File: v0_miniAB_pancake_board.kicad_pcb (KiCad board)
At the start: 2 copper layers, 51 x 37.4 mm, 13 parts, among them J1 Conn_01x04_Female, J10 Conn_01x03_Female, J11 Conn_01x03_Female, J2 Conn_01x02_Female, J3 Conn_01x02_Female, J4 Conn_01x02_Female, J5 Conn_01x02_Female, J6 Conn_01x02_Female, J7 Conn_01x03_Female, J8 Conn_01x03_Female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

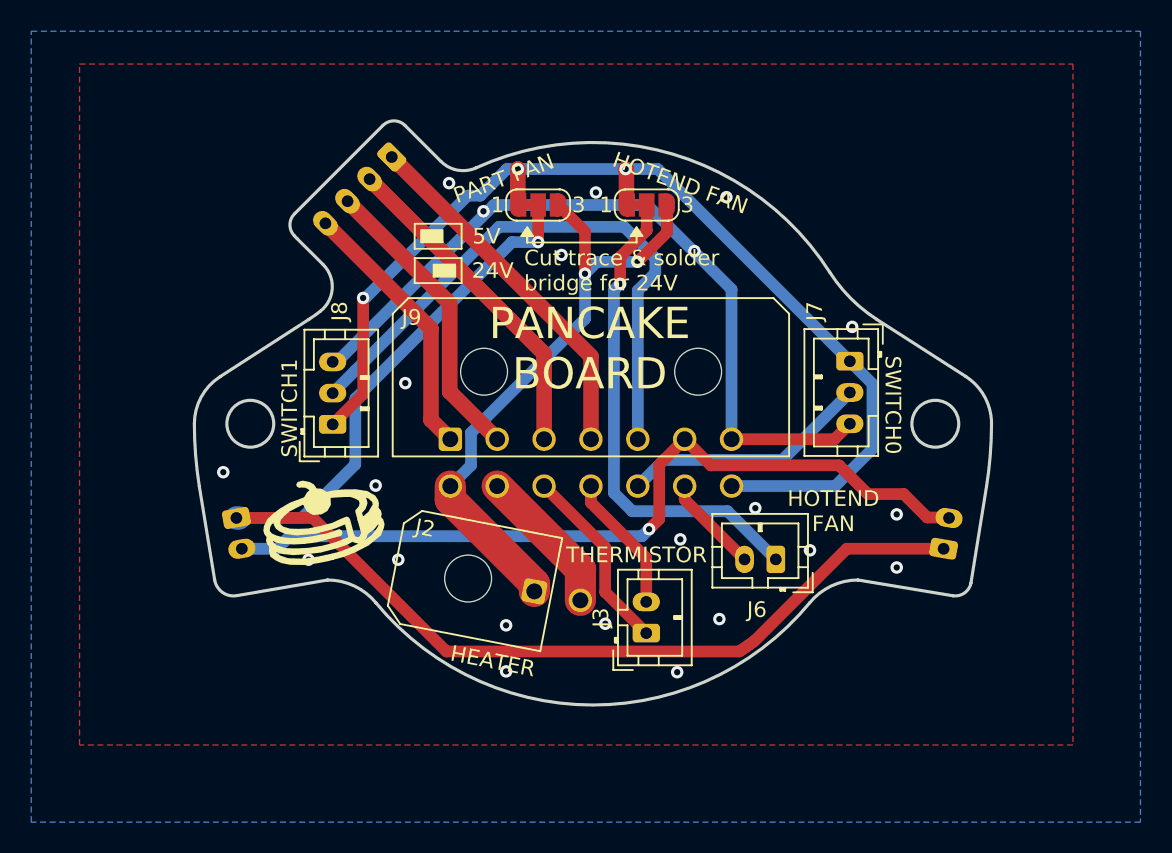
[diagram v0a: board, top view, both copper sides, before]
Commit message: Converted to KiCAD 6.0.0
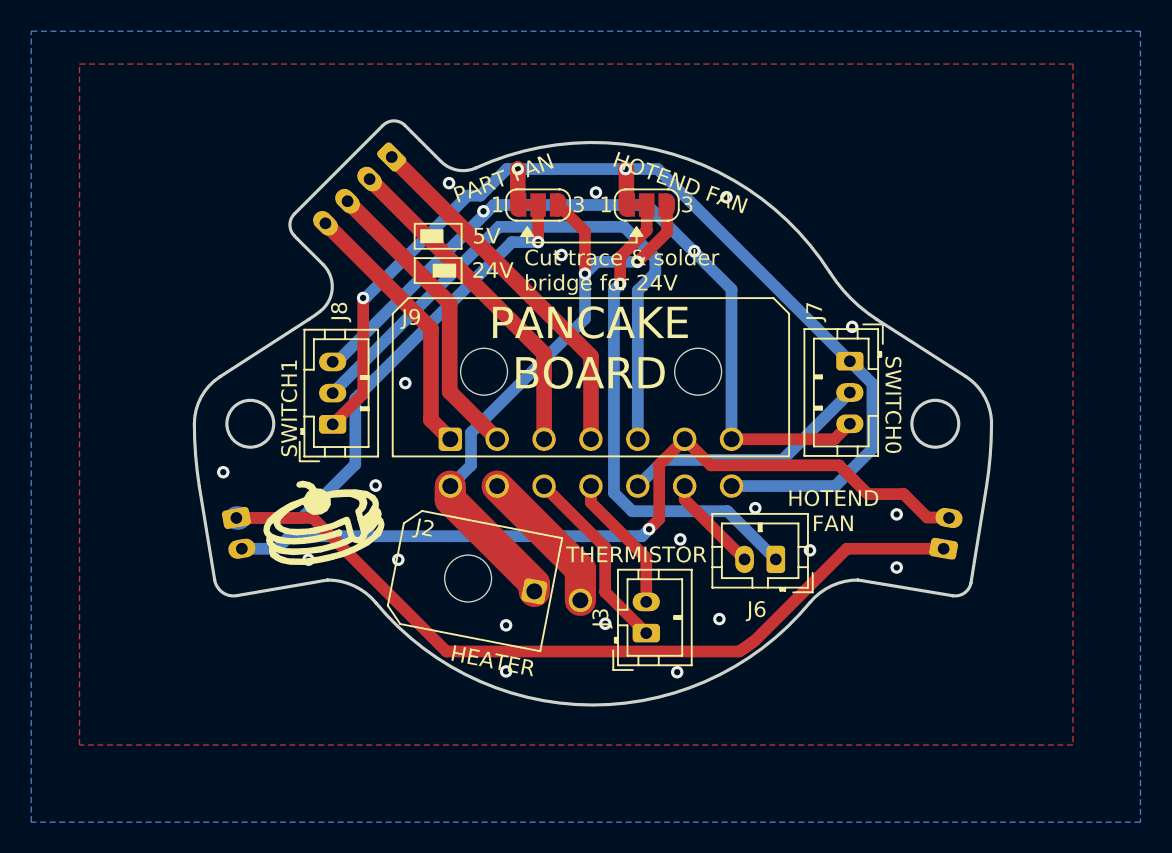
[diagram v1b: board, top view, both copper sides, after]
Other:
- net class Default removed

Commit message: First steps of the batboard conversion
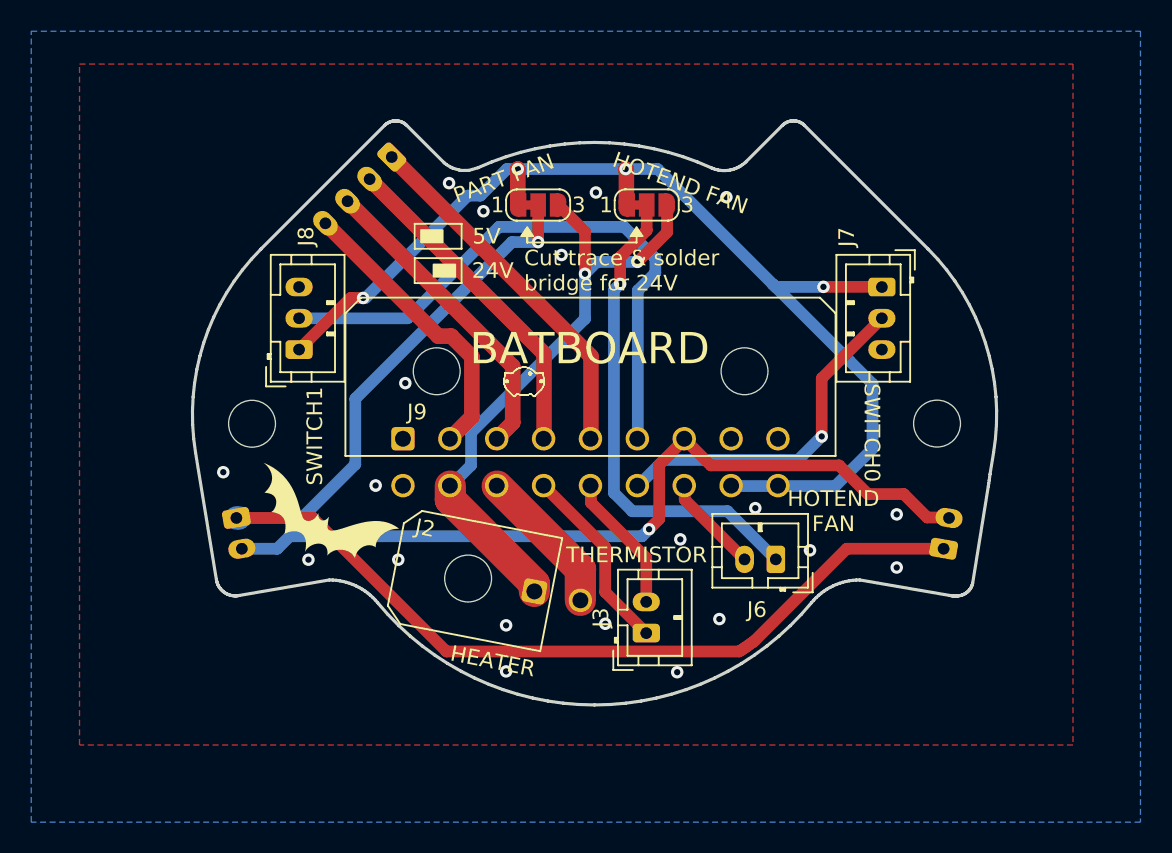
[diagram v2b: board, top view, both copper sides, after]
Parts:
- removed the REF** at (80.0, 110.7)
- removed the REF** at (89.4, 108.5)
- added REF**: MountingHole_3mm, MountingHole:MountingHole_3mm, F.Cu at (122.0, 100.0)
- added REF**: MountingHole_3mm, MountingHole:MountingHole_3mm, F.Cu at (78.2, 100.0)
- added svg2mod: G***, logos:Bat_Logo, F.Cu at (78.9, 101.2)
- added svg2mod: G***, logos:Bat_Logo, B.Cu at (90.5, 110.2)
- J9: footprint Connector_Molex:Molex_Micro-Fit_3.0_43045-1400_2x07_P3.00mm_Horizontal -> Connector_Molex:Molex_Micro-Fit_3.0_43045-1800_2x09_P3.00mm_Horizontal
- moved J8 5.25 mm to (81.2, 95.2)
- moved J7 5.17 mm to (118.5, 91.2)
- moved J9 3.03 mm to (87.8, 101.0)
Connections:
- J9 pad 1: /A+ -> unconnected-(J9-Pad1)
- J9 pad 10: /therm0 -> unconnected-(J9-Pad10)
- J9 pad 11: /therm1 -> +24V
- J9 pad 12: /sw0 -> /heat_gnd
- J9 pad 13: /fan1 -> /therm0
- J9 pad 14: +5V -> /therm1
- J9 pad 2: /A- -> /A+
- J9 pad 3: /B+ -> /A-
- J9 pad 4: /B- -> /B+
- J9 pad 5: /sw1 -> /B-
- J9 pad 6: /fan0 -> /sw1
- J9 pad 7: GND -> /fan0
- J9 pad 8: +24V -> GND
- J9 pad 9: /heat_gnd -> unconnected-(J9-Pad9)
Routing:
- net GND: track 49.6 -> 0.05 mm, vias 22 -> 20
- net /sw0: track 16.1 -> 22.2 mm, vias 0 -> 1
- net +5V: track 69.4 -> 73.0 mm, vias 3 -> 4
- net /A+: track 17.1 -> 18.7 mm
- net /A-: track 19.2 -> 20.0 mm
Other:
- board size 51 x 37.4 mm -> 51.5 x 37.4 mm
- board text added: "(based on Pancake by Christoph Mueller)"
- board text added: "BATBOARD"
- board text removed: "PANCAKE BOARD"
- board text removed: "christophmueller.org 2021"

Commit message: Further connections made
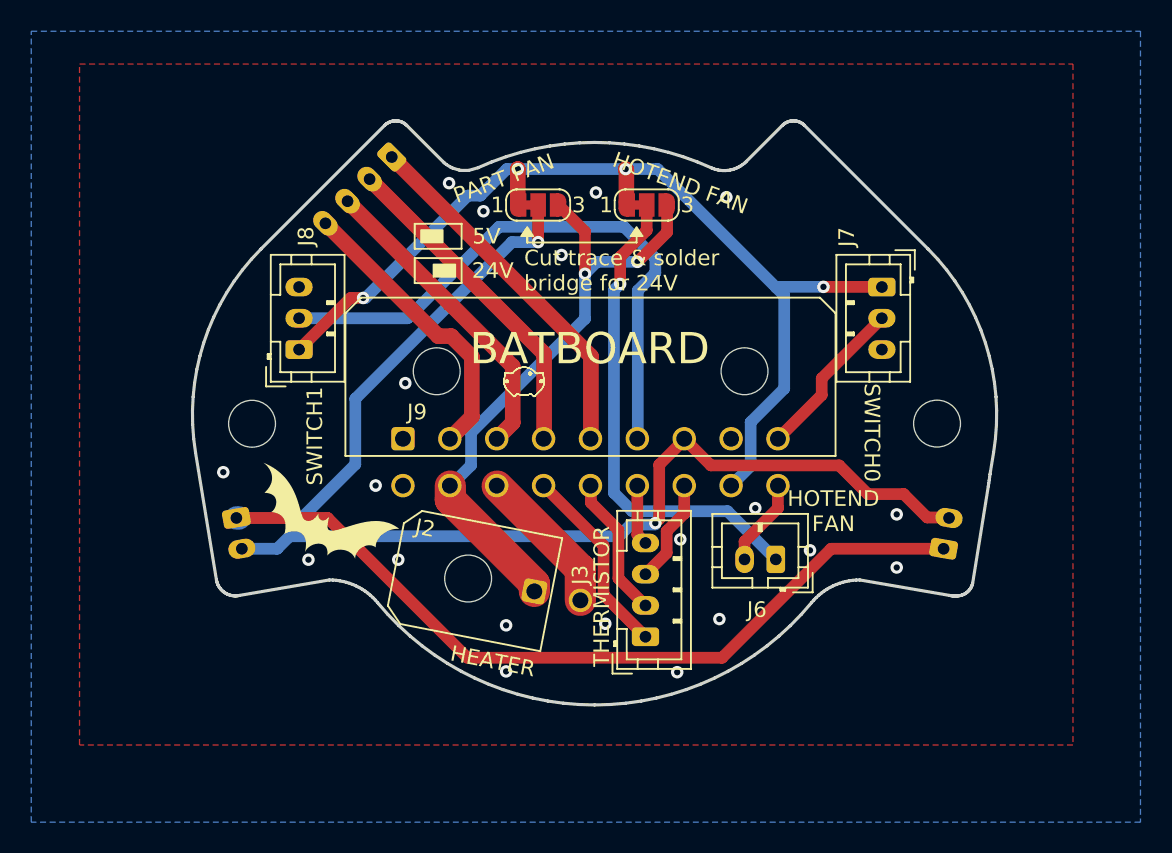
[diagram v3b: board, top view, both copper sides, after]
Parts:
- J3: value Conn_01x02_Female -> Conn_01x04_Female; footprint Connector_JST:JST_PH_B2B-PH-K_1x02_P2.00mm_Vertical -> Connector_JST:JST_PH_B4B-PH-K_1x04_P2.00mm_Vertical
- moved J3 0.24 mm to (103.4, 113.6)
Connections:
- J9 pad 15: /sw0 -> /therm3
- J9 pad 16: /fan1 -> /therm2
- J9 pad 18: unconnected-(J9-Pad18) -> /fan1
- J9 pad 9: unconnected-(J9-Pad9) -> /sw0
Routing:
- net /VFAN1: track 31.4 -> 0.00 mm, vias 1 -> 0
- net /fan0: track 52.3 -> 83.7 mm, vias 1 -> 2
- net /sw0: track 22.2 -> 10.5 mm, vias 1 -> 0
- net +5V: track 73.0 -> 64.0 mm
- net /therm2: track 0.00 -> 6.70 mm
- net /therm3: track 0.00 -> 3.89 mm
- net /fan1: track 6.28 -> 5.61 mm

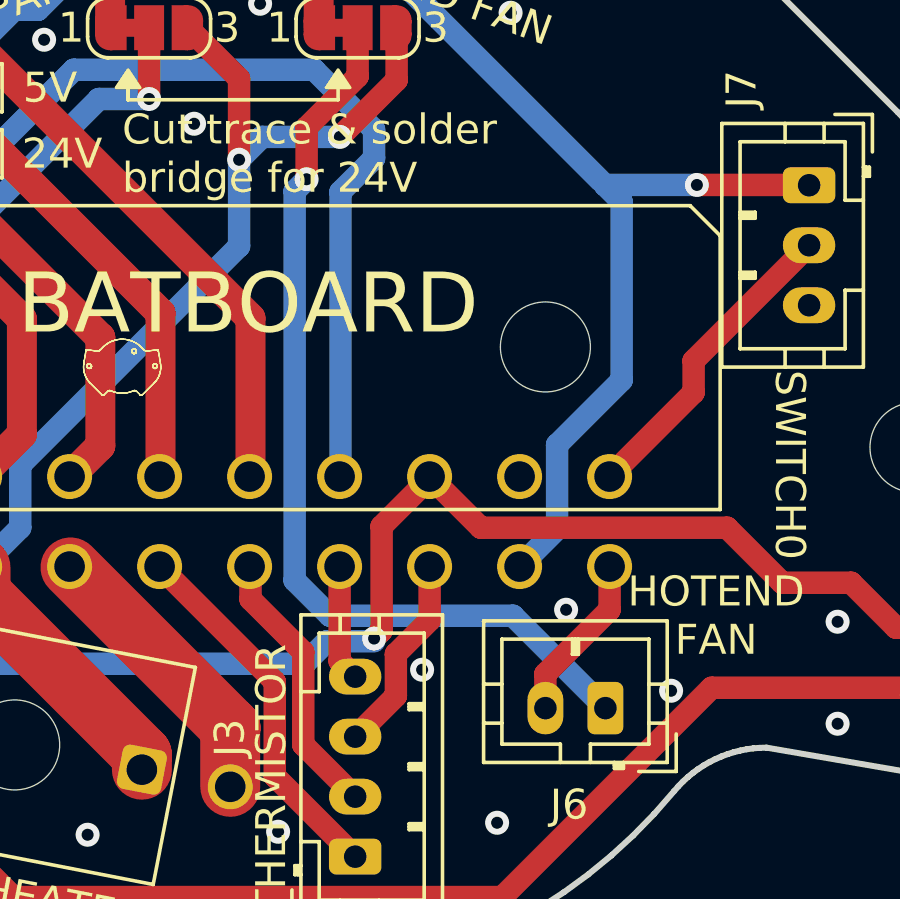
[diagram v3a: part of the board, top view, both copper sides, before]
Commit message: Fixed track to VFAN1
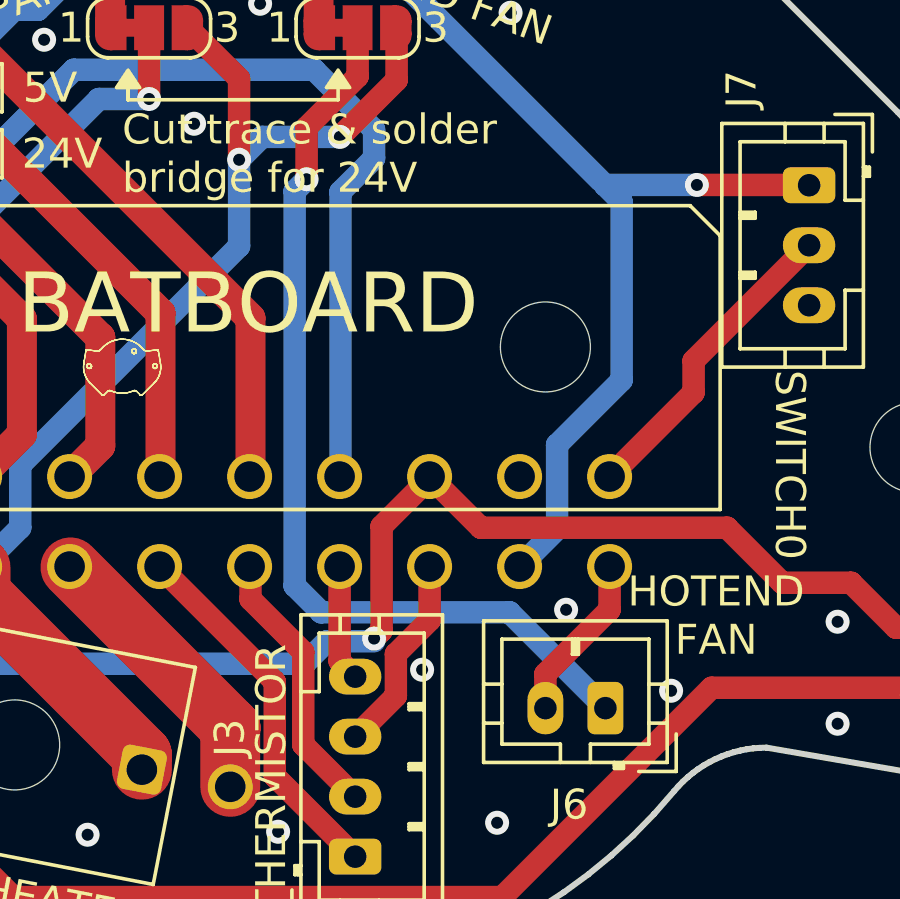
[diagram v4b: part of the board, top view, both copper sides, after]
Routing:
- net /VFAN1: track 0.00 -> 31.5 mm, vias 0 -> 1
- net /fan0: track 83.7 -> 52.3 mm, vias 2 -> 1
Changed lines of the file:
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@@
   (segment (start 117.6 104.5) (end 115.764999 102.664999) (width 0.75) (layer "F.Cu") (net 7))
   (segment (start 105.88 100.99) (end 104.249999 102.620001) (width 0.75) (layer "F.Cu") (net 7))
-  (segment (start 103.45 87.623401) (end 101.75 89.323401) (width 0.75) (layer "F.Cu") (net 7))
-  (segment (start 103.45 86) (end 103.45 87.623401) (width 0.75) (layer "F.Cu") (net 7))
   (segment (start 122.766912 106) (end 121.4 106) (width 0.75) (layer "F.Cu") (net 7))
   (segment (start 115.764999 102.664999) (end 107.554999 102.664999) (width 0.75) (layer "F.Cu") (net 7))
@@
   (segment (start 119.9 104.5) (end 117.6 104.5) (width 0.75) (layer "F.Cu") (net 7))
   (segment (start 122.797296 106.030384) (end 122.766912 106) (width 0.75) (layer "F.Cu") (net 7))
-  (segment (start 101.75 89.323401) (end 101.75 91.05) (width 0.75) (layer "F.Cu") (net 7))
   (segment (start 121.4 106) (end 119.9 104.5) (width 0.75) (layer "F.Cu") (net 7))
   (via (at 104 106.36) (size 0.8) (drill 0.4) (layers "F.Cu" "B.Cu") (net 7))
-  (via (at 101.75 91.05) (size 0.8) (drill 0.4) (layers "F.Cu" "B.Cu") (net 7))
   (segment (start 102.43048 106.44952) (end 104 106.44952) (width 0.75) (layer "B.Cu") (net 7))
-  (segment (start 101.350001 91.449999) (end 101.350001 104.421003) (width 0.75) (layer "B.Cu") (net 7))
-  (segment (start 101.350001 104.421003) (end 102.528998 105.6) (width 0.75) (layer "B.Cu") (net 7))
-  (segment (start 108.63 105.6) (end 111.71 108.68) (width 0.75) (layer "B.Cu") (net 7))
   (segment (start 80.6 107.2) (end 101.68 107.2) (width 0.75) (layer "B.Cu") (net 7))
-  (segment (start 102.528998 105.6) (end 108.63 105.6) (width 0.75) (layer "B.Cu") (net 7))
   (segment (start 101.68 107.2) (end 102.43048 106.44952) (width 0.75) (layer "B.Cu") (net 7))
   (segment (start 77.537296 107.999616) (end 79.800384 107.999616) (width 0.75) (layer "B.Cu") (net 7))
   (segment (start 79.800384 107.999616) (end 80.6 107.2) (width 0.75) (layer "B.Cu") (net 7))
-  (segment (start 101.75 91.05) (end 101.350001 91.449999) (width 0.75) (layer "B.Cu") (net 7))
   (segment (start 95.2 83.700006) (end 95.199994 83.7) (width 1) (layer "F.Cu") (net 8))
   (segment (start 118.49 91.24) (end 118.5 91.25) (width 0.75) (layer "F.Cu") (net 8))
@@
   (segment (start 84.80001 102.59999) (end 84.80001 98.39999) (width 0.75) (layer "B.Cu") (net 15))
   (segment (start 77.19 106.03) (end 77.36 106.03) (width 1.5) (layer "B.Cu") (net 15))
+  (segment (start 103.45 87.623401) (end 101.75 89.323401) (width 0.75) (layer "F.Cu") (net 16))
+  (segment (start 103.45 86) (end 103.45 87.623401) (width 0.75) (layer "F.Cu") (net 16))
+  (segment (start 101.75 89.323401) (end 101.75 91.05) (width 0.75) (layer "F.Cu") (net 16))
+  (via (at 101.75 91.05) (size 0.8) (drill 0.4) (layers "F.Cu" "B.Cu") (net 16))
+  (segment (start 108.515489 105.485489) (end 111.71 108.68) (width 0.75) (layer "B.Cu") (net 16))
+  (segment (start 102.235489 105.485489) (end 108.515489 105.485489) (width 0.75) (layer "B.Cu") (net 16))
+  (segment (start 101.350001 91.449999) (end 101.350001 104.600001) (width 0.75) (layer "B.Cu") (net 16))
+  (segment (start 101.75 91.05) (end 101.350001 91.449999) (width 0.75) (layer "B.Cu") (net 16))
+  (segment (start 101.350001 104.600001) (end 102.235489 105.485489) (width 0.75) (layer "B.Cu") (net 16))
   (segment (start 104.725489 106.874511) (end 105.85 105.75) (width 0.75) (layer "F.Cu") (net 19))
   (segment (start 103.37 109.63) (end 104.725489 108.274511) (width 0.75) (layer "F.Cu") (net 19))
